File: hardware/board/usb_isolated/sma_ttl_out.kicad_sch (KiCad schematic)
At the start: 8 parts, among them J7 Conn_Coaxial, U1 74LVCH2T45DC

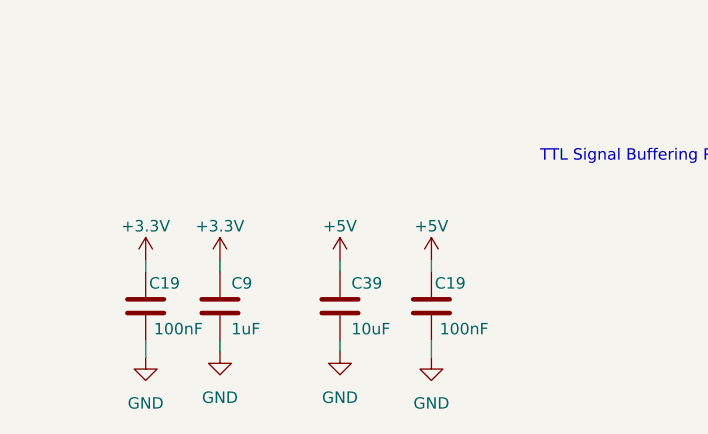
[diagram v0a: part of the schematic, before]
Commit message: update usb isolated pcba layout
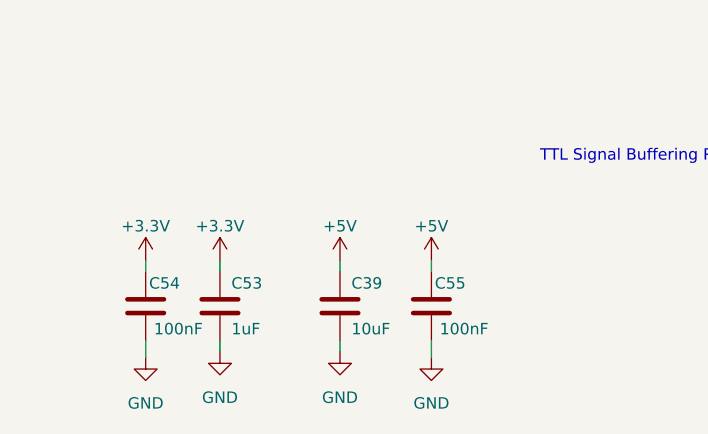
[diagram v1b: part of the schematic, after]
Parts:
- renumbered C9 to C53, C19 to C54, C19 to C55
